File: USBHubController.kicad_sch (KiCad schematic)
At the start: 16 parts, among them CN4 1-2199298-2, U1 TUSB4020BIPHPR

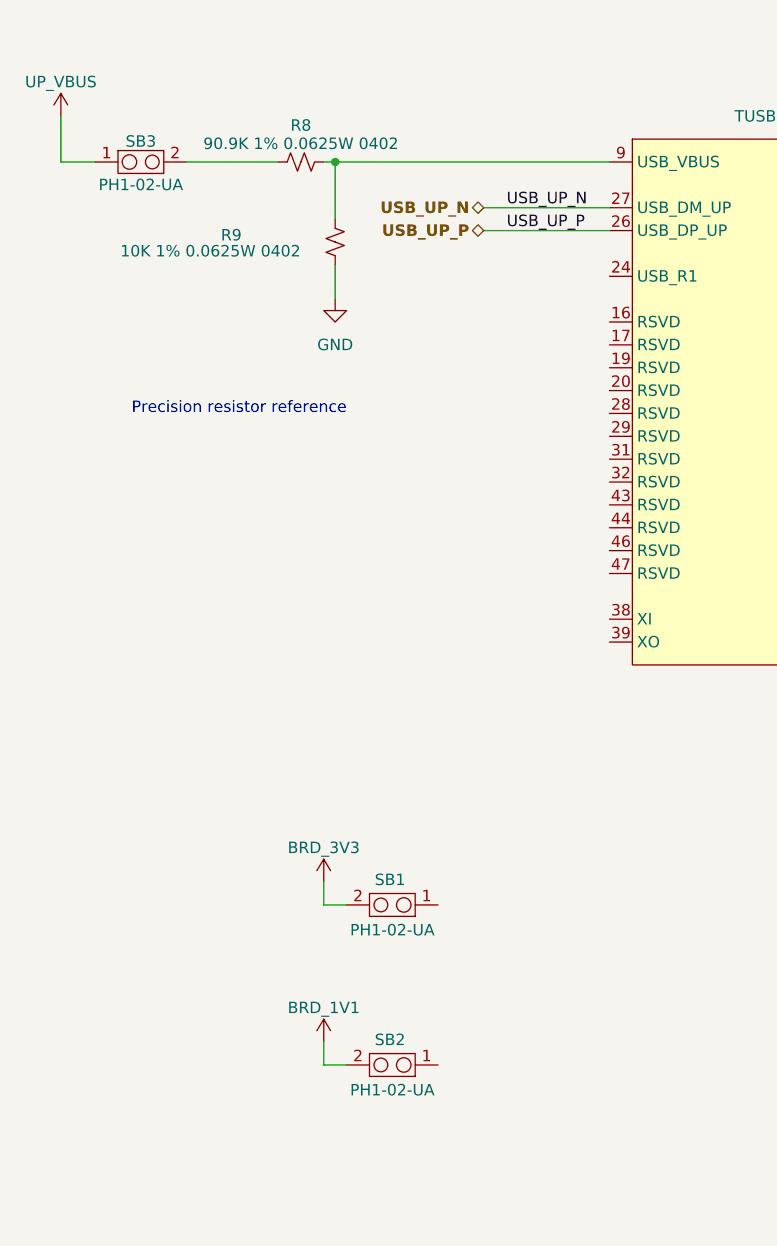
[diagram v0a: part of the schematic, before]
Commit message: 完成晶振电路
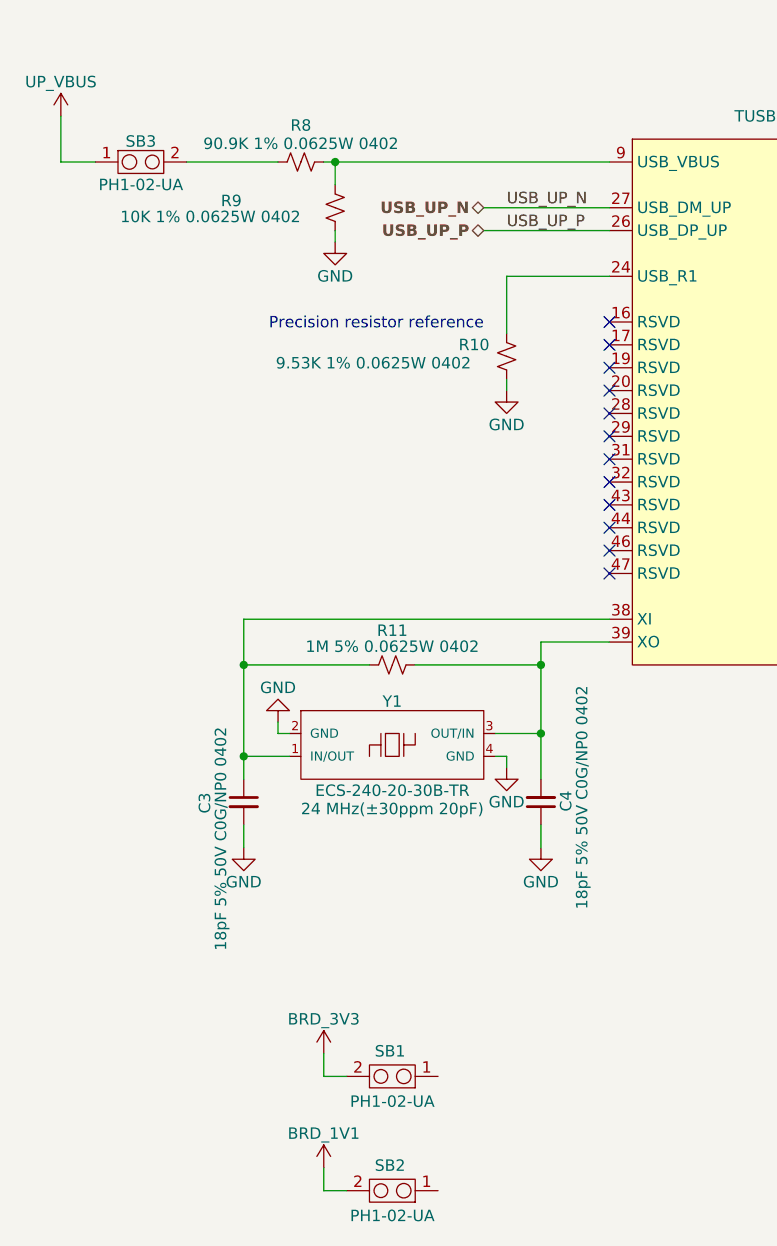
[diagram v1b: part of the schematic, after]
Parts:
- added C3, C4: 18pF 5% 50V C0G/NP0 0402, MY_Cap:AVX_C0402, symbol MY_Cap:KGM05ACG1H180JH
- added R10: 9.53K 1% 0.0625W 0402, MY_Res:YAGEO_R0402_Reflow, symbol MY_Res:AF0402FR-079K53L
- added R11: 1M 5% 0.0625W 0402, MY_Res:YAGEO_R0402_Reflow, symbol MY_Res:AF0402JR-071ML
- added Y1: 24 MHz(±30ppm 20pF), MY_Osc:XTAL_ECS-240-20-30B-TR, symbol MY_Osc:ECS-240-20-30B-TR
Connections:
- net GND: now also C3.2, C4.1, R10.2, Y1.2 (GND), Y1.4 (GND)
- net at U1.24 (USB_R1): now also R10.1
- net at U1.38 (XI): now also C3.1, R11.2, Y1.1 (IN/OUT)
- net at U1.39 (XO): now also C4.2, R11.1, Y1.3 (OUT/IN)
- no-connect marks 0 -> 12
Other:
- moved on the sheet: R9, SB1, SB2

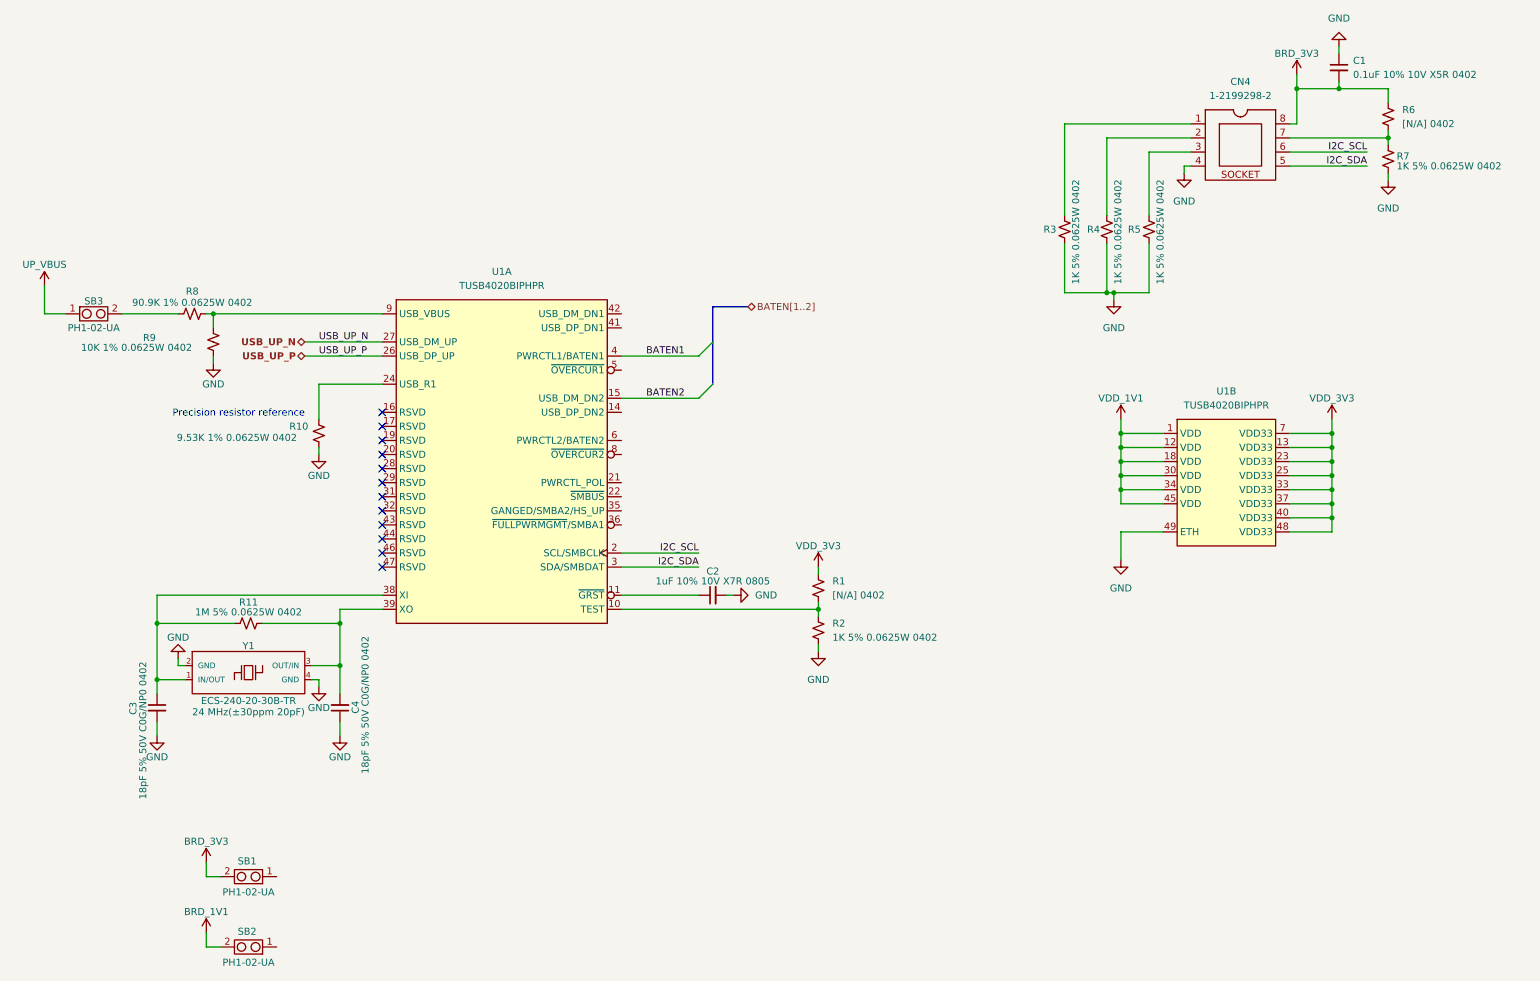
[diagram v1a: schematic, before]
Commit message: 完成 USBHub Controller 原理图
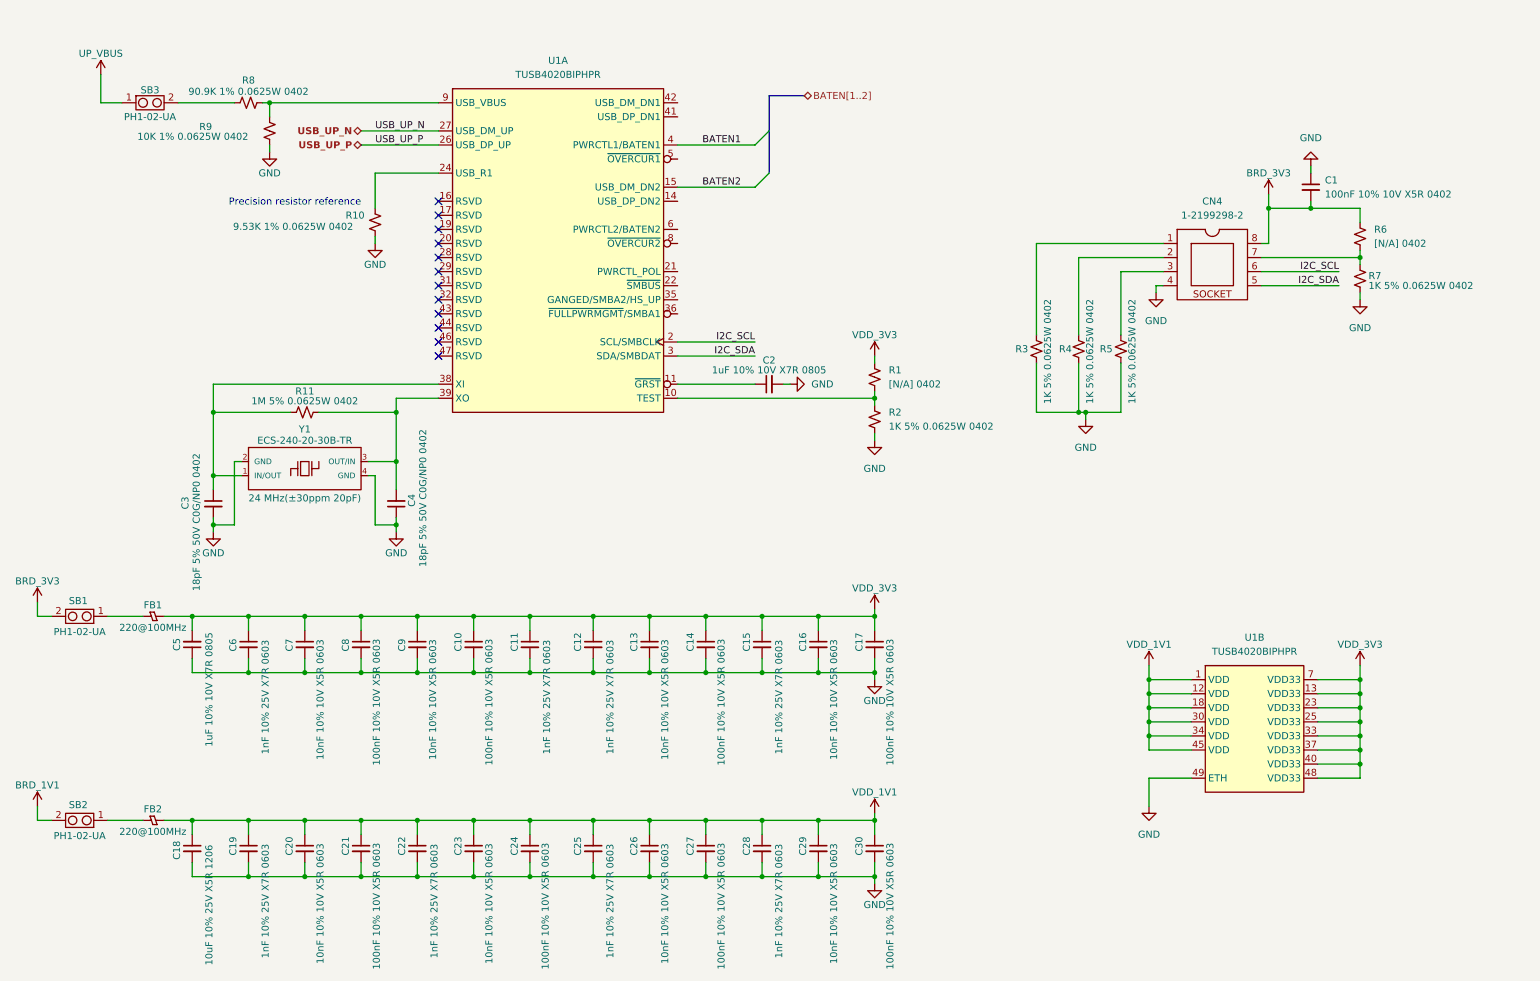
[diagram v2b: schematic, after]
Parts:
- added C10, C14, C17, C21, C24, C27, C30, C8: 100nF 10% 10V X5R 0603, MY_Cap:TDK_C0603_C, symbol MY_Cap:C0603X5R1A104K030BC
- added C11, C12, C15, C19, C22, C25, C28, C6: 1nF 10% 25V X7R 0603, MY_Cap:TDK_C0603_C, symbol MY_Cap:C0603X7R1E102K030BA
- added C13, C16, C20, C23, C26, C29, C7, C9: 10nF 10% 10V X5R 0603, MY_Cap:TDK_C0603_C, symbol MY_Cap:C0603X5R1A103K030BA
- added C18: 10uF 10% 25V X5R 1206, MY_Cap:muRata_GRM31_C1206, symbol MY_Cap:GRM319R61E106KA12D
- added C5: 1uF 10% 10V X7R 0805, MY_Cap:YAGEO_C0805_Reflow_A, symbol MY_Cap:AC0805KKX7R6BB105
- added FB1, FB2: 220@100MHz, MY_FB:BEADC1608X95N, symbol MY_FB:BLM18PG221SN1D
- C1: value 0.1uF 10% 10V X5R 0402 -> 100nF 10% 10V X5R 0402
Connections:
- net GND: now also C10.2, C11.2, C12.2, C13.2, C14.2, C15.2, C16.2, C17.2, C18.2, C19.2, C20.2, C21.2, C22.2, C23.2, C24.2, C25.2, C26.2, C27.2, C28.2, C29.2, C30.2, C5.1, C6.2, C7.2, C8.2, C9.2
- net VDD_1V1: now also C18.1, C19.1, C20.1, C21.1, C22.1, C23.1, C24.1, C25.1, C26.1, C27.1, C28.1, C29.1, C30.1, FB2.2
- net VDD_3V3: now also C10.1, C11.1, C12.1, C13.1, C14.1, C15.1, C16.1, C17.1, C5.2, C6.1, C7.1, C8.1, C9.1, FB1.2
- net at SB1.1: now also FB1.1
- net at SB2.1: now also FB2.1
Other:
- moved on the sheet: C1, C2, C3, C4, CN4, R1, R10, R11, R2, R3, R4, R5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
